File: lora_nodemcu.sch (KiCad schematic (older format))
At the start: 12 parts, among them U1 RFM95, U2 LM1117-3.3, U3 WeMos_mini

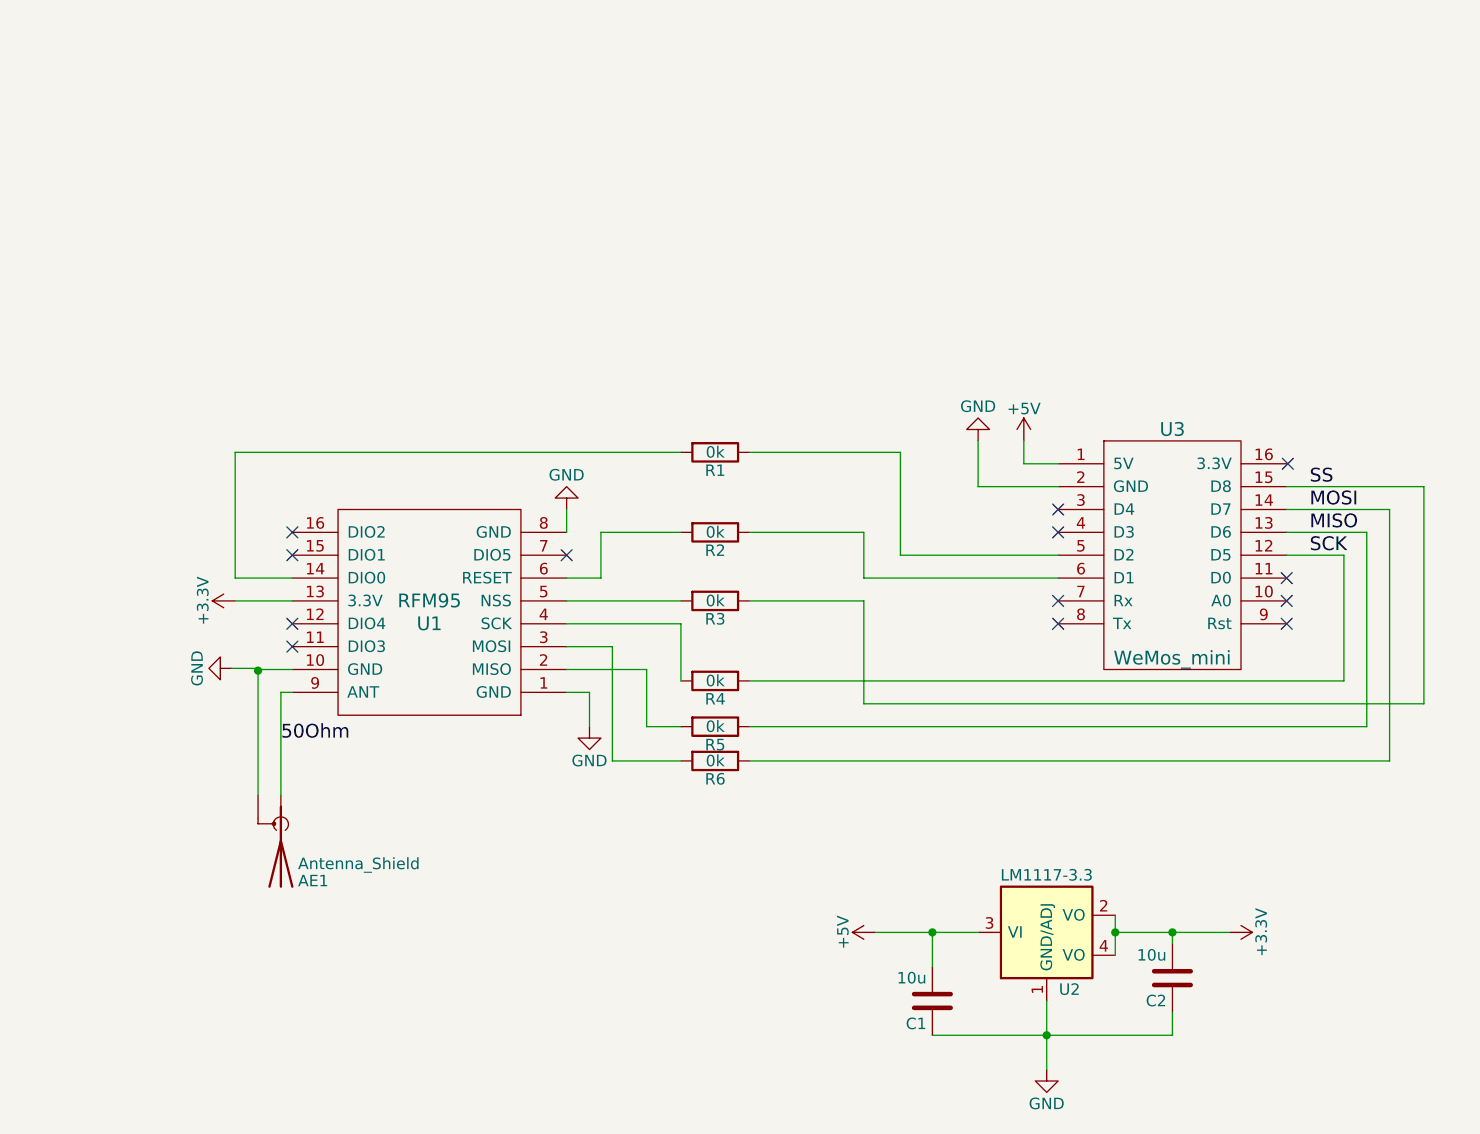
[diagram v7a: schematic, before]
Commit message: Added new caps and connection points.
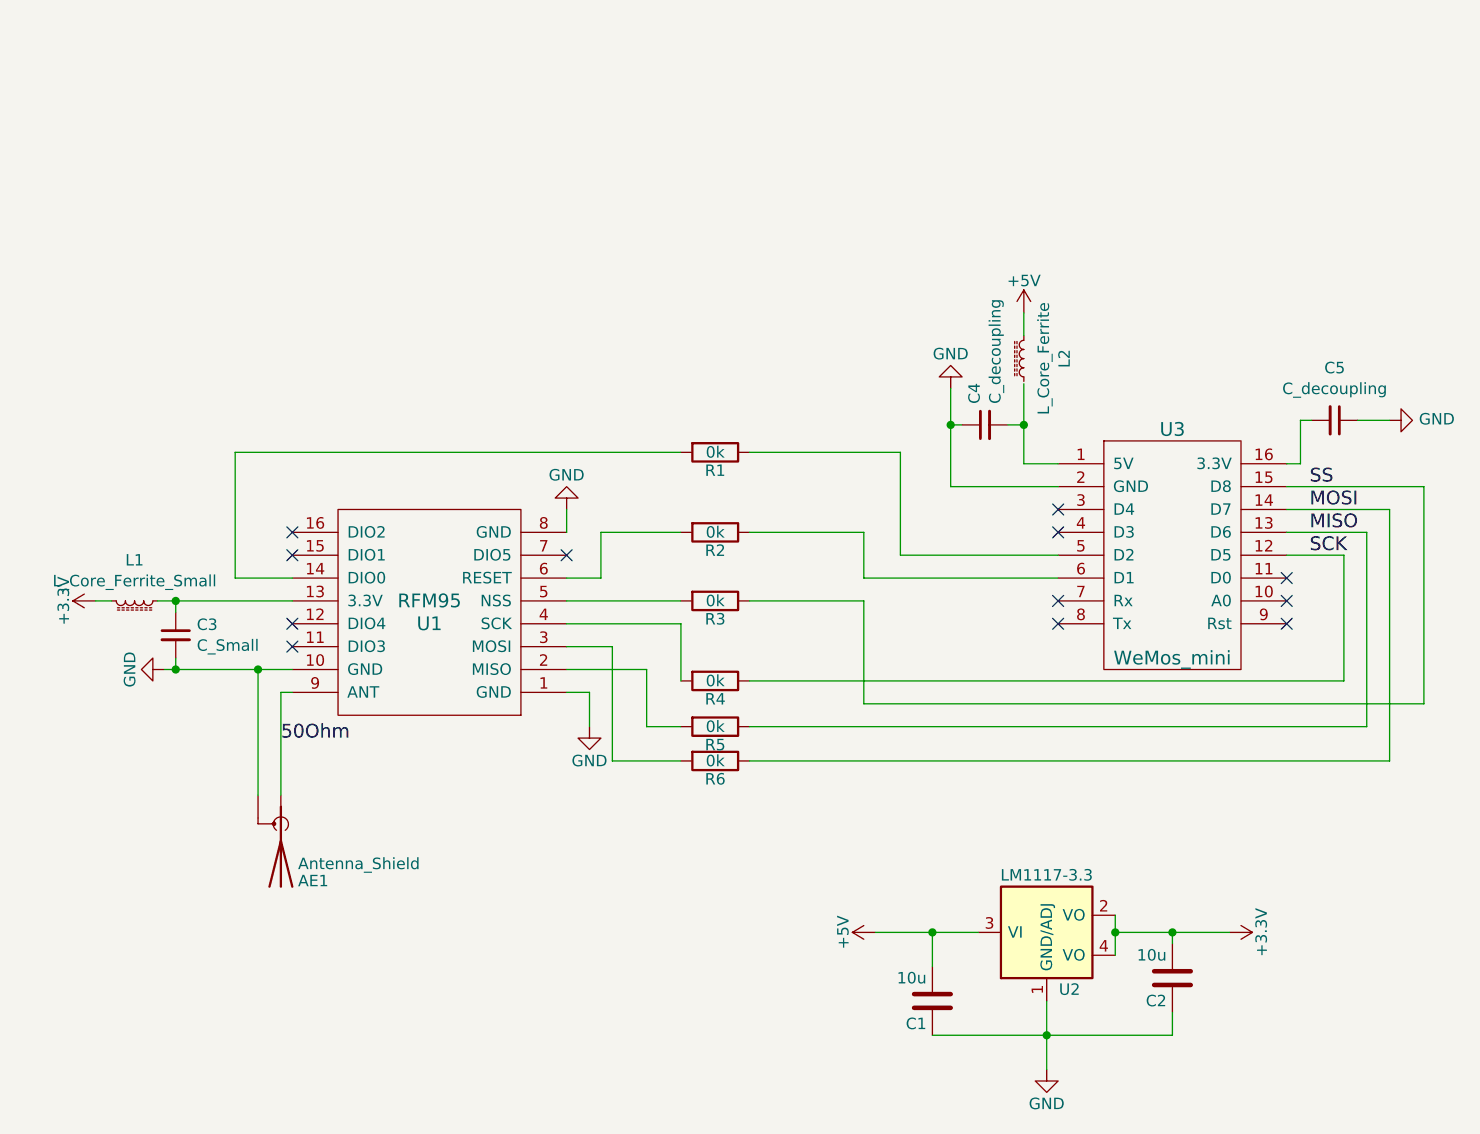
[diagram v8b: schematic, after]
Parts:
- added C3: C_Small, Capacitors_SMD:C_0805_HandSoldering, symbol device:C_Small
- added C4, C5: C_decoupling, Capacitors_SMD:C_0805_HandSoldering, symbol device:C_Small
- added L1: L_Core_Ferrite_Small, Inductors_SMD:L_0805_HandSoldering, symbol device:L_Core_Ferrite_Small
- added L2: L_Core_Ferrite, Inductors_SMD:L_0805_HandSoldering, symbol device:L_Core_Ferrite_Small
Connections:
- net +3V3: now also L1.2; no longer U1.13 (3.3V)
- net +5V: now also L2.2; no longer U3.1 (5V)
- net GND: now also U1.10 (GND), C3.2, C4.1, C5.1
- net at U3.16 (3.3V): now also C5.2
- new net: C3.1, L1.1, U1.13 (3.3V)
- new net: C4.2, U3.1 (5V)
- no-connect marks 13 -> 12
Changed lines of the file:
@@
 L power:+3.3V #PWR03
 U 1 1 59CB1055
-P 4250 3100
-F 0 "#PWR03" H 4250 2950 50  0001 C CNN
-F 1 "+3.3V" H 4250 3240 50  0000 C CNN
-F 2 "" H 4250 3100 50  0001 C CNN
-F 3 "" H 4250 3100 50  0001 C CNN
-	1    4250 3100
+P 3640 3100
+F 0 "#PWR03" H 3640 2950 50  0001 C CNN
+F 1 "+3.3V" H 3640 3240 50  0000 C CNN
+F 2 "" H 3640 3100 50  0001 C CNN
+F 3 "" H 3640 3100 50  0001 C CNN
+	1    3640 3100
 	0    -1   -1   0
 $EndComp
@@
 L power:+5V #PWR07
 U 1 1 59DAD071
-P 7700 2400
-F 0 "#PWR07" H 7700 2250 50  0001 C CNN
-F 1 "+5V" H 7700 2540 50  0000 C CNN
-F 2 "" H 7700 2400 50  0001 C CNN
-F 3 "" H 7700 2400 50  0001 C CNN
-	1    7700 2400
+P 7700 1840
+F 0 "#PWR07" H 7700 1690 50  0001 C CNN
+F 1 "+5V" H 7700 1980 50  0000 C CNN
+F 2 "" H 7700 1840 50  0001 C CNN
+F 3 "" H 7700 1840 50  0001 C CNN
+	1    7700 1840
 	1    0    0    -1
 $EndComp
@@
 L power:GND #PWR08
 U 1 1 59DAD0A3
-P 7500 2400
-F 0 "#PWR08" H 7500 2150 50  0001 C CNN
-F 1 "GND" H 7500 2250 50  0000 C CNN
-F 2 "" H 7500 2400 50  0001 C CNN
-F 3 "" H 7500 2400 50  0001 C CNN
-	1    7500 2400
+P 7380 2170
+F 0 "#PWR08" H 7380 1920 50  0001 C CNN
+F 1 "GND" H 7380 2020 50  0000 C CNN
+F 2 "" H 7380 2170 50  0001 C CNN
+F 3 "" H 7380 2170 50  0001 C CNN
+	1    7380 2170
 	-1   0    0    1
 $EndComp
@@
 L power:GND #PWR09
 U 1 1 59E595E3
-P 4235 3395
-F 0 "#PWR09" H 4235 3145 50  0001 C CNN
-F 1 "GND" H 4235 3245 50  0000 C CNN
-F 2 "" H 4235 3395 50  0001 C CNN
-F 3 "" H 4235 3395 50  0001 C CNN
-	1    4235 3395
-	0    1    1    0
-$EndComp
-Wire Wire Line
-	4500 3500 4450 3500
-Wire Wire Line
-	4450 3500 4450 3950
-Wire Wire Line
-	4500 3400 4350 3400
-Wire Wire Line
-	5700 3500 5800 3500
-Wire Wire Line
-	5800 3500 5800 3650
-Wire Wire Line
-	4500 3100 4250 3100
-Wire Wire Line
-	4350 3395 4350 3950
-Wire Wire Line
-	5900 3300 5700 3300
-Wire Wire Line
-	5700 3400 6050 3400
-Wire Wire Line
-	5700 3100 6200 3100
-Wire Wire Line
-	5850 3000 5700 3000
-Wire Wire Line
-	4500 3000 4250 3000
-Wire Wire Line
-	6050 3400 6050 3650
-Wire Wire Line
-	5700 3200 6200 3200
-Wire Wire Line
-	6200 3200 6200 3450
-Wire Wire Line
-	6200 2800 5850 2800
-Wire Wire Line
-	6200 2450 4250 2450
-Wire Wire Line
-	4250 2450 4250 3000
-Wire Wire Line
-	5700 2800 5700 2700
-Wire Wire Line
-	7700 2400 7700 2500
-Wire Wire Line
-	7700 2500 7850 2500
-Wire Wire Line
-	7500 2400 7500 2600
-Wire Wire Line
-	7500 2600 7850 2600
-Wire Wire Line
-	8850 2600 9450 2600
-Wire Wire Line
-	7000 3550 9450 3550
-Wire Wire Line
-	7000 3100 6500 3100
-Wire Wire Line
-	8850 2700 9300 2700
-Wire Wire Line
-	9300 3800 6500 3800
-Wire Wire Line
-	8850 2900 9100 2900
-Wire Wire Line
-	5900 3300 5900 3800
-Wire Wire Line
-	5900 3800 6200 3800
-Wire Wire Line
-	5850 2800 5850 3000
-Wire Wire Line
-	9300 2700 9300 3800
-Wire Wire Line
-	8850 2800 9200 2800
-Wire Wire Line
-	9200 2800 9200 3650
-Wire Wire Line
-	9100 2900 9100 3450
-Wire Wire Line
-	9100 3450 6500 3450
-Wire Wire Line
-	9200 3650 6500 3650
-Wire Wire Line
-	6050 3650 6200 3650
-Wire Wire Line
-	9450 3550 9450 2600
-Wire Wire Line
-	7000 3550 7000 3100
-Wire Wire Line
-	8100 4550 8600 4550
-Wire Wire Line
-	7050 4550 7500 4550
-Wire Wire Line
-	7800 4850 7800 5150
-Wire Wire Line
-	7300 4700 7300 4550
-Connection ~ 7300 4550
-Wire Wire Line
-	8350 4550 8350 4600
-Connection ~ 8350 4550
-Wire Wire Line
-	7300 5000 8350 5000
-Wire Wire Line
-	8350 5000 8350 4900
-Connection ~ 7800 5000
-Wire Wire Line
-	8100 4475 8100 4650
-Connection ~ 8100 4550
-Connection ~ 4350 3405
-Wire Wire Line
-	4235 3395 4350 3395
+P 3940 3400
+F 0 "#PWR09" H 3940 3150 50  0001 C CNN
+F 1 "GND" H 3940 3250 50  0000 C CNN
+F 2 "" H 3940 3400 50  0001 C CNN
+F 3 "" H 3940 3400 50  0001 C CNN
+	1    3940 3400
+	0    1    1    0
+$EndComp
 NoConn ~ 7850 2800
-NoConn ~ 8855 2500
-Wire Wire Line
-	7160 2450 6500 2450
-Wire Wire Line
-	7850 3000 7000 3000
-Wire Wire Line
-	7000 3000 7000 2800
-Wire Wire Line
-	7000 2800 6500 2800
-Wire Wire Line
-	7160 2450 7160 2900
-Wire Wire Line
-	7160 2900 7850 2900
 NoConn ~ 7850 2700
 Text Label 4450 3720 0    60   ~ 0
 50Ohm
+$Comp
+L device:C_Small C4
+U 1 1 5A1CF19C
+P 7530 2330
+F 0 "C4" H 7622 2376 50  0000 L CNN
+F 1 "C_decoupling" H 7622 2285 50  0000 L CNN
+F 2 "Capacitors_SMD:C_0805_HandSoldering" H 7530 2330 50  0001 C CNN
+F 3 "" H 7530 2330 50  0001 C CNN
+	1    7530 2330
+	0    -1   -1   0
+$EndComp
+$Comp
+L device:L_Core_Ferrite_Small L2
+U 1 1 5A1CF7A6
+P 7700 2040
+F 0 "L2" V 7522 2040 50  0000 C CNN
+F 1 "L_Core_Ferrite" V 7613 2040 50  0000 C CNN
+F 2 "Inductors_SMD:L_0805_HandSoldering" H 7700 2040 50  0001 C CNN
+F 3 "" H 7700 2040 50  0001 C CNN
+	1    7700 2040
+	-1   0    0    1
+$EndComp
+$Comp
+L device:C_Small C3
+U 1 1 5A1DF95C
+P 3990 3250
+F 0 "C3" H 4082 3296 50  0000 L CNN
+F 1 "C_Small" H 4082 3205 50  0000 L CNN
+F 2 "Capacitors_SMD:C_0805_HandSoldering" H 3990 3250 50  0001 C CNN
+F 3 "" H 3990 3250 50  0001 C CNN
+	1    3990 3250
+	1    0    0    -1
+$EndComp
+$Comp
+L device:L_Core_Ferrite_Small L1
+U 1 1 5A1DFA59
+P 3810 3100
+F 0 "L1" V 3632 3100 50  0000 C CNN
+F 1 "L_Core_Ferrite_Small" V 3723 3100 50  0000 C CNN
+F 2 "Inductors_SMD:L_0805_HandSoldering" H 3810 3100 50  0001 C CNN
+F 3 "" H 3810 3100 50  0001 C CNN
+	1    3810 3100
+	0    1    1    0
+$EndComp
+Wire Wire Line
+	4500 3500 4450 3500
+Wire Wire Line
+	4450 3500 4450 3950
+Wire Wire Line
+	3940 3400 4500 3400
+Wire Wire Line
+	5700 3500 5800 3500
+Wire Wire Line
+	5800 3500 5800 3650
+Wire Wire Line
+	3910 3100 4500 3100
+Wire Wire Line
+	5900 3300 5700 3300
+Wire Wire Line
+	5700 3400 6050 3400
+Wire Wire Line
+	5700 3100 6200 3100
+Wire Wire Line
+	5850 3000 5700 3000
+Wire Wire Line
+	4500 3000 4250 3000
+Wire Wire Line
+	6050 3400 6050 3650
+Wire Wire Line
+	5700 3200 6200 3200
+Wire Wire Line
+	6200 3200 6200 3450
+Wire Wire Line
+	6200 2800 5850 2800
+Wire Wire Line
+	6200 2450 4250 2450
+Wire Wire Line
+	4250 2450 4250 3000
+Wire Wire Line
+	5700 2800 5700 2700
+Wire Wire Line
+	7700 2150 7700 2500
+Wire Wire Line
+	7700 2500 7850 2500
+Wire Wire Line
+	7380 2600 7850 2600
+Wire Wire Line
+	8850 2600 9450 2600
+Wire Wire Line
+	7000 3550 9450 3550
+Wire Wire Line
+	7000 3100 6500 3100
+Wire Wire Line
+	8850 2700 9300 2700
+Wire Wire Line
+	9300 3800 6500 3800
+Wire Wire Line
+	8850 2900 9100 2900
+Wire Wire Line
+	5900 3300 5900 3800
+Wire Wire Line
+	5900 3800 6200 3800
+Wire Wire Line
+	5850 2800 5850 3000
+Wire Wire Line
+	9300 2700 9300 3800
+Wire Wire Line
+	8850 2800 9200 2800
+Wire Wire Line
+	9200 2800 9200 3650
+Wire Wire Line
+	9100 2900 9100 3450
+Wire Wire Line
+	9100 3450 6500 3450
+Wire Wire Line
+	9200 3650 6500 3650
+Wire Wire Line
+	6050 3650 6200 3650
+Wire Wire Line
+	9450 3550 9450 2600
+Wire Wire Line
+	7000 3550 7000 3100
+Wire Wire Line
+	8100 4550 8600 4550
+Wire Wire Line
+	7050 4550 7500 4550
+Wire Wire Line
+	7800 4850 7800 5150
+Wire Wire Line
+	7300 4700 7300 4550
+Connection ~ 7300 4550
+Wire Wire Line
+	8350 4550 8350 4600
+Connection ~ 8350 4550
+Wire Wire Line
+	7300 5000 8350 5000
+Wire Wire Line
+	8350 5000 8350 4900
+Connection ~ 7800 5000
+Wire Wire Line
+	8100 4475 8100 4650
+Connection ~ 8100 4550
+Wire Wire Line
+	7160 2450 6500 2450
+Wire Wire Line
+	7850 3000 7000 3000
+Wire Wire Line
+	7000 3000 7000 2800
+Wire Wire Line
+	7000 2800 6500 2800
+Wire Wire Line
+	7160 2450 7160 2900
+Wire Wire Line
+	7160 2900 7850 2900
+Wire Wire Line
+	7380 2600 7380 2170
+Wire Wire Line
+	7700 1840 7700 1940
+Wire Wire Line
+	7700 2330 7630 2330
+Connection ~ 7700 2330
+Wire Wire Line
+	7430 2330 7380 2330
+Connection ~ 7380 2330
+Wire Wire Line
+	3710 3100 3640 3100
+Wire Wire Line
+	3990 3350 3990 3400
+Connection ~ 3990 3400
+Wire Wire Line
+	3990 3150 3990 3100
+Connection ~ 3990 3100
+$Comp
+L device:C_Small C5
+U 1 1 5A1F028E
+P 9060 2310
+F 0 "C5" V 8831 2310 50  0000 C CNN
+F 1 "C_decoupling" V 8922 2310 50  0000 C CNN
+F 2 "Capacitors_SMD:C_0805_HandSoldering" H 9060 2310 50  0001 C CNN
+F 3 "" H 9060 2310 50  0001 C CNN
+	1    9060 2310
+	0    1    1    0
+$EndComp
+Wire Wire Line
+	8850 2500 8910 2500
+Wire Wire Line
+	8910 2500 8910 2310
+Wire Wire Line
+	8910 2310 8960 2310
+$Comp
+L power:GND #PWR010
+U 1 1 5A1F2C89
+P 9300 2310
+F 0 "#PWR010" H 9300 2060 50  0001 C CNN
+F 1 "GND" V 9305 2182 50  0000 R CNN
+F 2 "" H 9300 2310 50  0001 C CNN
+F 3 "" H 9300 2310 50  0001 C CNN
+	1    9300 2310
+	0    -1   -1   0
+$EndComp
+Wire Wire Line
+	9300 2310 9160 2310
+Wire Wire Line
+	4350 3950 4350 3400
+Connection ~ 4350 3400
 $EndSCHEMATC
